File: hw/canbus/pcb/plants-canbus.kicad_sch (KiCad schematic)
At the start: 21 parts, among them J1 Conn_01x02_Male, J2 Sensor, J3 Mini-DIN-6, J4 Mini-DIN-6, Q1 2N3904, Q2 S8550, Q3 2N3904, Q4 S8550, SW1 SW_Reset, U1 ATtiny85V-10P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

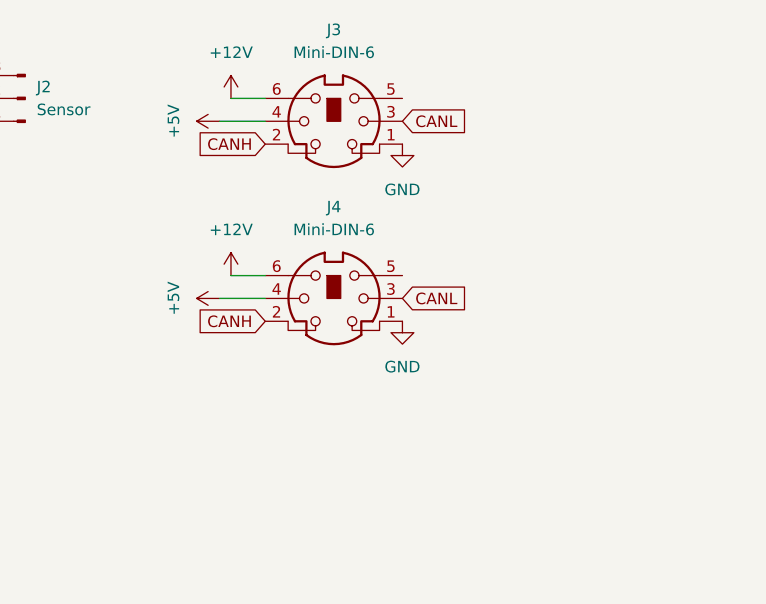
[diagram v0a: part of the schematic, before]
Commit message: Replace PS/2 connector with RJ12
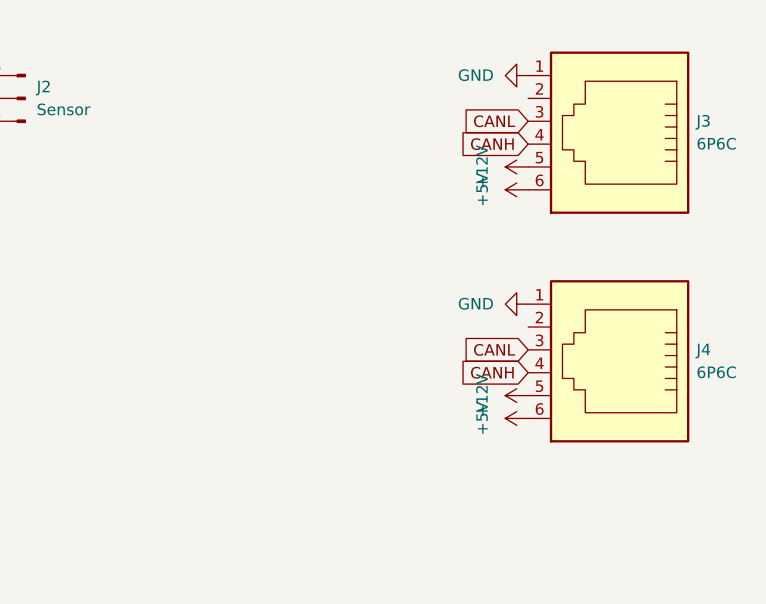
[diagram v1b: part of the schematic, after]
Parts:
- removed J3, J4: Mini-DIN-6, Footprints:Connector_MiniDIN_6, symbol Connector:Mini-DIN-6
- added J3, J4: 6P6C, Footprints:RJ12_Pulse_E5566, symbol Connector:6P6C
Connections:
- net +12V: now also J3.5, J4.5
- net +5V: now also J3.6, J4.6
- net CANH: now also J3.4, J4.4
- net CANL: now also J3.3, J4.3
- net GND: now also J3.1, J4.1
